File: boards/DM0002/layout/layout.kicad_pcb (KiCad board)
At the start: 4 copper layers, 15 x 43.6 mm, 70 parts, among them J1 62201021121, J2 USB4105-GF-A, SW1 KMR231G LFS, U1 TLV75801PDRVR, U2 W25Q16JVUXIQ, U3 RP2040, U4 SG-210STF 12.0000ML0, U5 TXB0102DCUR, U6 TXB0102DCUR, U7 TLV9001IDBVR

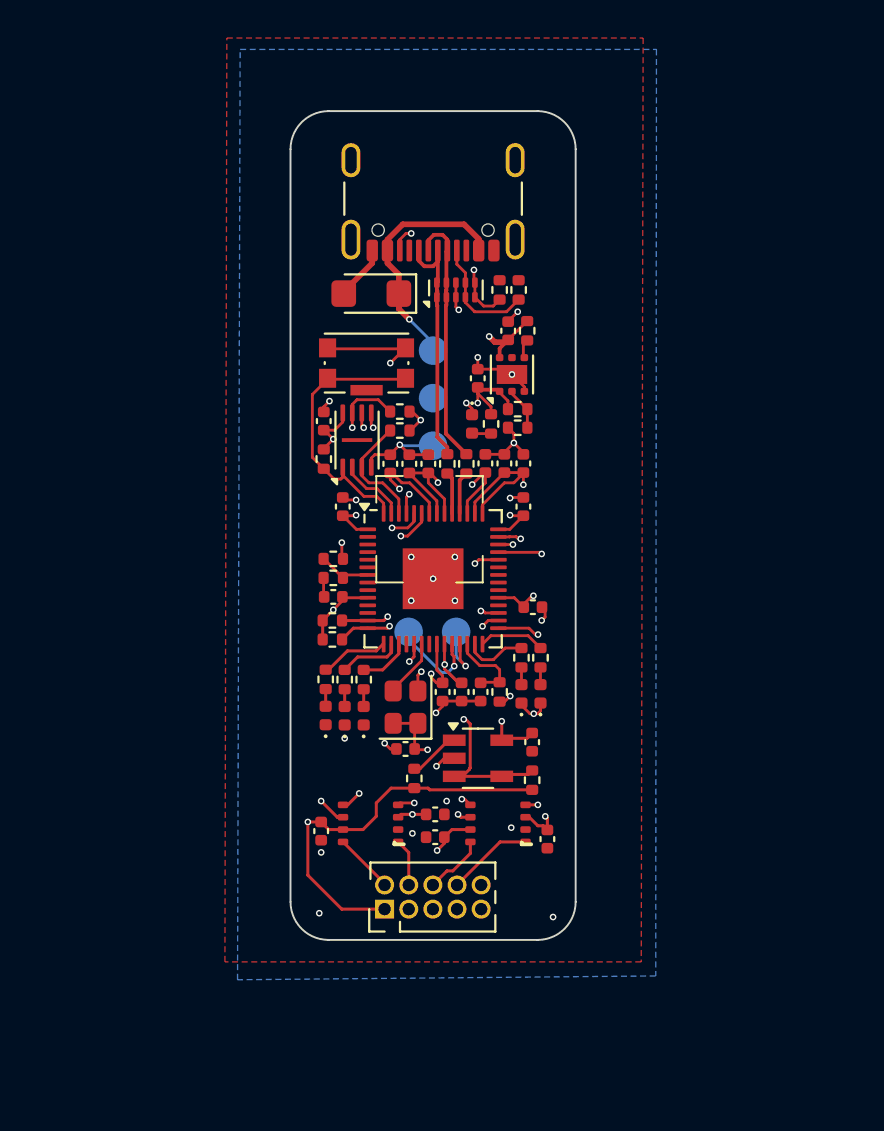
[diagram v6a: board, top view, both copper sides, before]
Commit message: SMT header added to sch and layout
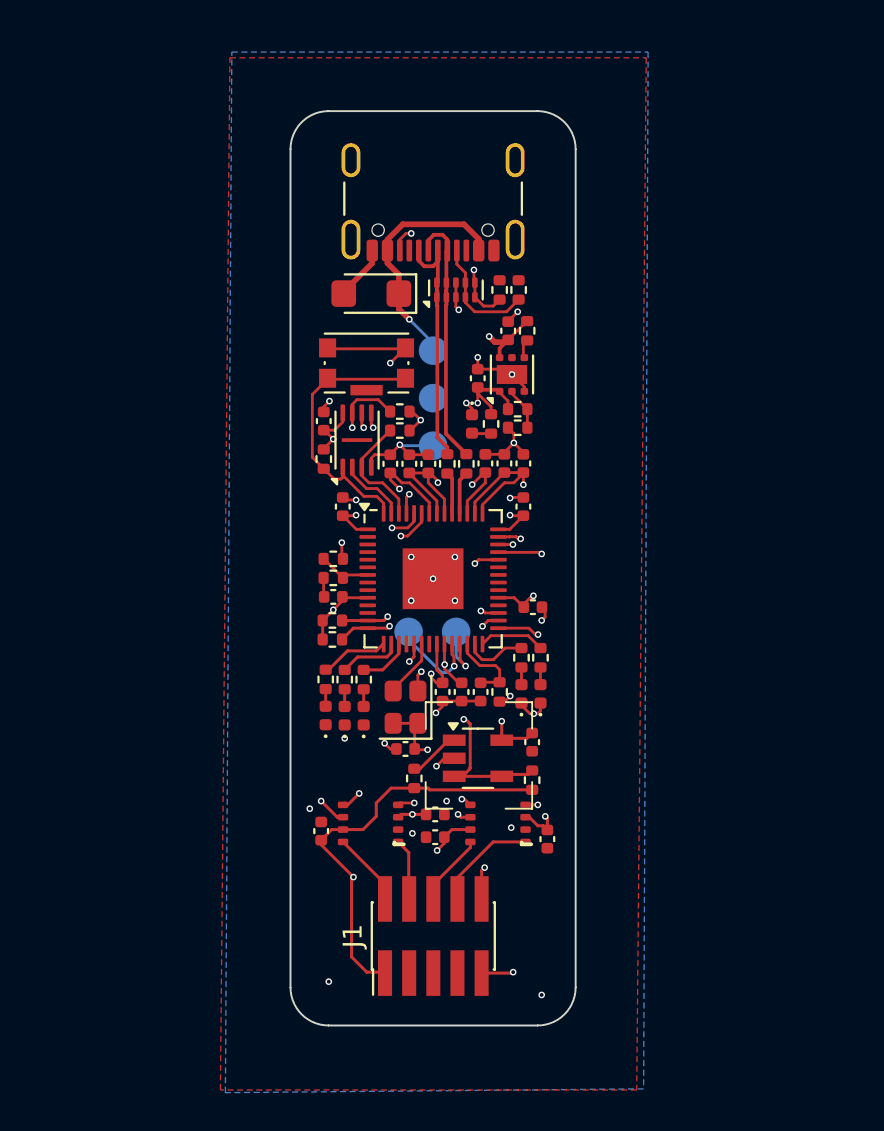
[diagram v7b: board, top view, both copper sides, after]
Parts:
- J1: value 62201021121 -> FTSH-105-01-L-DV-K-A; footprint PinHeader_2x05_P1.27mm_Vertical:PinHeader_2x05_P1.27mm_Vertical -> FTSH-105-01-L-DV-K-A:FTSH-105-01-L-DV-K-A
- moved V1 12.2 mm to (43.3, 80.7)
- moved J1 2.93 mm to (40.4, 86.8)
- moved TP1 2.52 mm to (46.0, 86.9)
- turned C2 to 90 degrees
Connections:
- net SWD_HEADER.NC_PH_Pin_7 renamed SWD_HEADER.NC_FTSH-105-01-L-DV-K-A_P7
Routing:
- net TARGET_GND_DETECT: track 24.1 -> 27.4 mm, vias 1 -> 2
- net TARGET_VDDIO: track 31.1 -> 29.1 mm
- net TARGET_RESET: track 18.8 -> 19.9 mm, vias 1 -> 2
- net MCU.VDD_1V1: track 25.0 -> 23.9 mm
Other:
- board size 15 x 43.6 mm -> 15 x 48.1 mm
